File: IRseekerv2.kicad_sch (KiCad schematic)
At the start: 49 parts, among them J13 Conn_01x04_Pin, J14 Conn_01x02_Pin, J15 SEL_VOLTAGE, J16 G, J17 G, J18 G, J19 G, J20 Conn_01x02_Pin, J26 Conn_01x02_Pin, J27 Conn_01x02_Pin, J28 Conn_01x02_Pin, SW1 SW_Push, SW2 SW_Push, U10 TSSP4038, U11 TSSP4038, U12 TSSP4038, U13 TSSP4038, U14 TSSP4038, U15 TSSP4038, U16 TSSP4038, U17 AMS1117-3.3, U2 HEF4082BT, U3 STM32G431CBUx, U4 HEF4082BT, U5 TSSP4038, U6 TSSP4038, U7 TSSP4038, U8 TSSP4038, U9 TSSP4038, Y1 Crystal

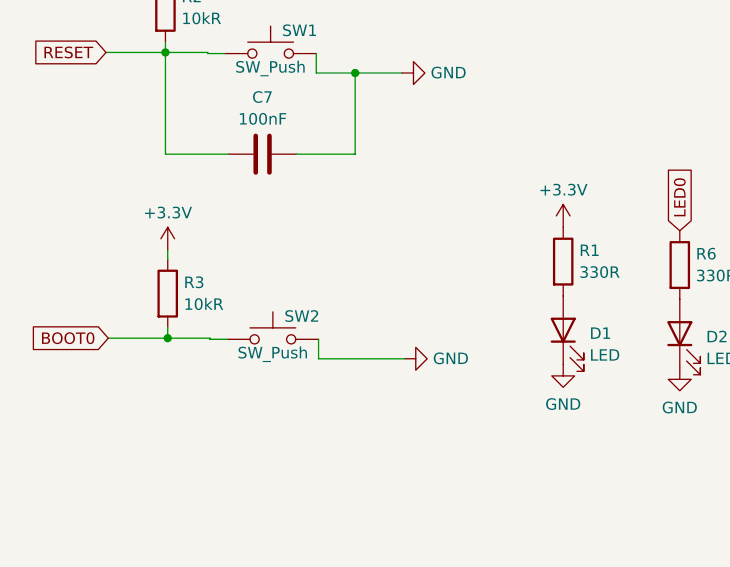
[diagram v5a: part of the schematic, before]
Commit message: BOOT0 pulldown instead of pullup
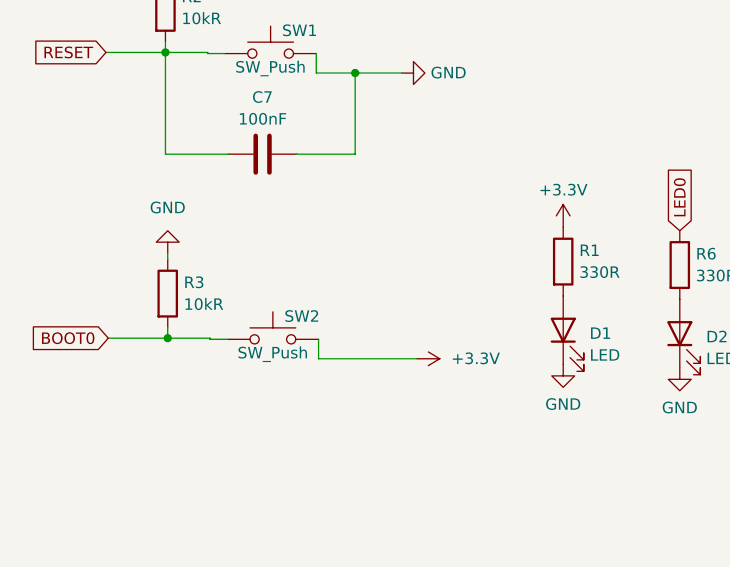
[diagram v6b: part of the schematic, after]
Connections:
- net +3.3V: now also SW2.2; no longer R3.1
- net GND: now also R3.1; no longer SW2.2
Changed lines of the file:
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@@
+    (stroke (width 0) (type default))
+  )
+  (wire (pts (xy 38.354 66.04) (xy 38.354 66.675))
     (stroke (width 0) (type default))
   )
@@
     (stroke (width 0) (type default))
   )
-  (wire (pts (xy 55.118 77.724) (xy 64.643 77.724))
+  (wire (pts (xy 55.118 77.724) (xy 66.04 77.724))
     (stroke (width 0) (type default))
   )
@@
   )
   (wire (pts (xy 226.695 149.479) (xy 226.695 158.623))
-    (stroke (width 0) (type default))
-  )
-  (wire (pts (xy 38.354 65.659) (xy 38.354 66.675))
     (stroke (width 0) (type default))
   )
@@
     )
   )
-  (symbol (lib_id "power:GND") (at 64.643 77.724 90) (unit 1)
-    (in_bom yes) (on_board yes) (dnp no) (fields_autoplaced)
-    (property "Reference" "#PWR017" (at 70.993 77.724 0)
-      (effects (font (size 1.27 1.27)) hide)
-    )
-    (property "Value" "GND" (at 67.818 77.724 90)
-      (effects (font (size 1.27 1.27)) (justify right))
-    )
-    (property "Footprint" "" (at 64.643 77.724 0)
-      (effects (font (size 1.27 1.27)) hide)
-    )
-    (property "Datasheet" "" (at 64.643 77.724 0)
-      (effects (font (size 1.27 1.27)) hide)
-    )
-    (pin "1")
-    (instances
-      (project "IRseekerv2"
-        (path "/c83ed66b-8f4f-4f32-bd83-eab9fc6ed48e"
-          (reference "#PWR017") (unit 1)
-        )
-      )
-    )
-  )
   (symbol (lib_id "Sensor_Proximity:TSSP58038") (at 257.937 139.192 270) (unit 1)
     (in_bom yes) (on_board yes) (dnp no) (fields_autoplaced)
@@
     )
   )
-  (symbol (lib_id "power:+3.3V") (at 38.354 65.659 0) (unit 1)
-    (in_bom yes) (on_board yes) (dnp no) (fields_autoplaced)
-    (property "Reference" "#PWR016" (at 38.354 69.469 0)
-      (effects (font (size 1.27 1.27)) hide)
-    )
-    (property "Value" "+3.3V" (at 38.354 61.5259 0)
-      (effects (font (size 1.27 1.27)))
-    )
-    (property "Footprint" "" (at 38.354 65.659 0)
-      (effects (font (size 1.27 1.27)) hide)
-    )
-    (property "Datasheet" "" (at 38.354 65.659 0)
+  (symbol (lib_id "power:+3.3V") (at 66.04 77.724 270) (unit 1)
+    (in_bom yes) (on_board yes) (dnp no) (fields_autoplaced)
+    (property "Reference" "#PWR016" (at 62.23 77.724 0)
+      (effects (font (size 1.27 1.27)) hide)
+    )
+    (property "Value" "+3.3V" (at 69.85 77.724 90)
+      (effects (font (size 1.27 1.27)) (justify left))
+    )
+    (property "Footprint" "" (at 66.04 77.724 0)
+      (effects (font (size 1.27 1.27)) hide)
+    )
+    (property "Datasheet" "" (at 66.04 77.724 0)
       (effects (font (size 1.27 1.27)) hide)
     )
@@
         )
       )
+    )
+  )
+  (symbol (lib_id "power:GND") (at 38.354 66.04 180) (unit 1)
+    (in_bom yes) (on_board yes) (dnp no) (fields_autoplaced)
+    (property "Reference" "#PWR027" (at 38.354 59.69 0)
+      (effects (font (size 1.27 1.27)) hide)
+    )
+    (property "Value" "GND" (at 38.354 60.96 0)
+      (effects (font (size 1.27 1.27)))
+    )
+    (property "Footprint" "" (at 38.354 66.04 0)
+      (effects (font (size 1.27 1.27)) hide)
+    )
+    (property "Datasheet" "" (at 38.354 66.04 0)
+      (effects (font (size 1.27 1.27)) hide)
+    )
+    (pin "1")
+    (instances
+      (project "IRseekerv2"
+        (path "/c83ed66b-8f4f-4f32-bd83-eab9fc6ed48e"
+          (reference "#PWR027") (unit 1)
+        )
+      )

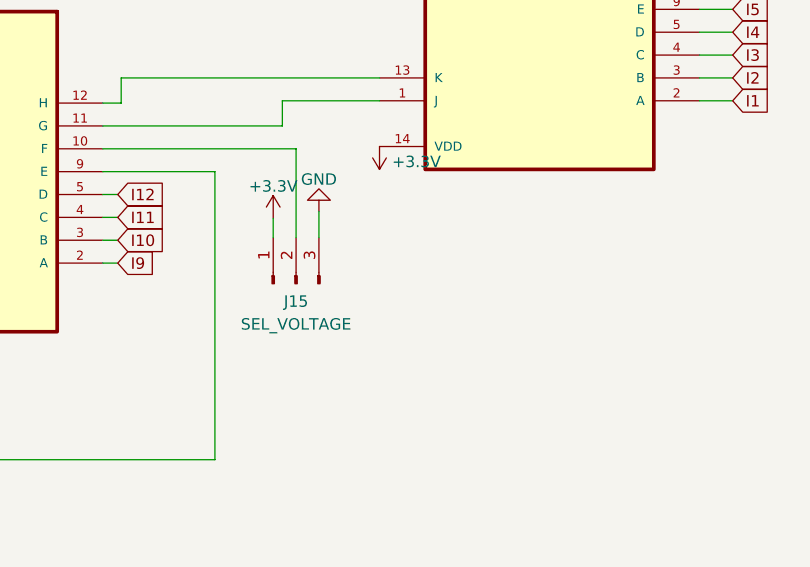
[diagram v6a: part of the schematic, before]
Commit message: removed SEL_VOlTAGE and added OUTGATE pin out
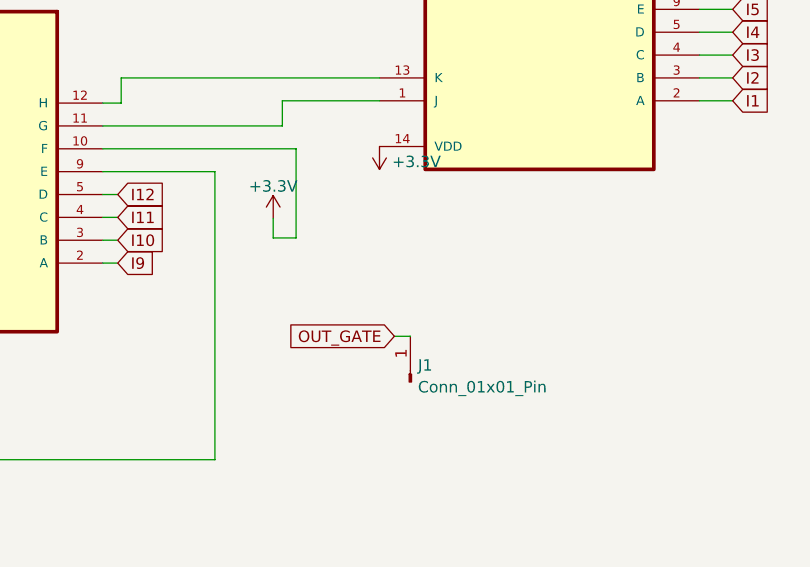
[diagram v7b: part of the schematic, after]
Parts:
- removed J15: SEL_VOLTAGE, Connector_PinHeader_2.54mm:PinHeader_1x03_P2.54mm_Vertical, symbol Connector:Conn_01x03_Male
- added J1: Conn_01x01_Pin, Connector_PinHeader_2.54mm:PinHeader_1x01_P2.54mm_Vertical, symbol Connector:Conn_01x01_Pin
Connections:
- net +3.3V: now also U2.10 (F)
- net OUT_GATE: now also J1.1 (Pin_1)
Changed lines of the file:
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@@
-    (stroke (width 0) (type default))
-  )
-  (wire (pts (xy 162.687 204.089) (xy 162.687 207.01))
     (stroke (width 0) (type default))
   )
@@
     (stroke (width 0) (type default))
   )
+  (wire (pts (xy 160.147 197.104) (xy 160.147 207.01))
+    (stroke (width 0) (type default))
+  )
   (wire (pts (xy 138.684 192.024) (xy 140.716 192.024))
     (stroke (width 0) (type default))
@@
     (stroke (width 0) (type default))
   )
+  (wire (pts (xy 171.069 217.932) (xy 172.847 217.932))
+    (stroke (width 0) (type default))
+  )
   (wire (pts (xy 329.946 94.742) (xy 329.946 93.98))
     (stroke (width 0) (type default))
@@
     (stroke (width 0) (type default))
   )
+  (wire (pts (xy 160.147 207.01) (xy 157.607 207.01))
+    (stroke (width 0) (type default))
+  )
   (wire (pts (xy 380.873 151.257) (xy 380.873 170.688))
     (stroke (width 0) (type default))
@@
     (stroke (width 0) (type default))
   )
-  (wire (pts (xy 160.147 197.104) (xy 160.147 207.01))
-    (stroke (width 0) (type default))
-  )
   (wire (pts (xy 165.1 67.31) (xy 177.8 67.31))
     (stroke (width 0) (type default))
@@
     (property "Intersheetrefs" "${INTERSHEET_REFS}" (at 362.4944 168.5766 0)
       (effects (font (size 1.27 1.27)) (justify left) hide)
+    )
+  )
+  (global_label "OUT_GATE" (shape input) (at 171.069 217.932 180) (fields_autoplaced)
+    (effects (font (size 1.27 1.27)) (justify right))
+    (property "Intersheetrefs" "${INTERSHEET_REFS}" (at 159.5845 217.8526 0)
+      (effects (font (size 1.27 1.27)) (justify right) hide)
     )
   )
@@
     )
   )
+  (symbol (lib_id "Connector:Conn_01x01_Pin") (at 172.847 223.012 90) (unit 1)
+    (in_bom yes) (on_board yes) (dnp no) (fields_autoplaced)
+    (property "Reference" "J1" (at 173.6852 221.1649 90)
+      (effects (font (size 1.27 1.27)) (justify right))
+    )
+    (property "Value" "Conn_01x01_Pin" (at 173.6852 223.5891 90)
+      (effects (font (size 1.27 1.27)) (justify right))
+    )
+    (property "Footprint" "Connector_PinHeader_2.54mm:PinHeader_1x01_P2.54mm_Vertical" (at 172.847 223.012 0)
+      (effects (font (size 1.27 1.27)) hide)
+    )
+    (property "Datasheet" "~" (at 172.847 223.012 0)
+      (effects (font (size 1.27 1.27)) hide)
+    )
+    (pin "1")
+    (instances
+      (project "IRseekerv2"
+        (path "/c83ed66b-8f4f-4f32-bd83-eab9fc6ed48e"
+          (reference "J1") (unit 1)
+        )
+      )
+    )
+  )
   (symbol (lib_id "power:+3.3V") (at 150.876 100.203 0) (unit 1)
     (in_bom yes) (on_board yes) (dnp no) (fields_autoplaced)
@@
         (path "/c83ed66b-8f4f-4f32-bd83-eab9fc6ed48e"
           (reference "#PWR0114") (unit 1)
-        )
-      )
-    )
-  )
-  (symbol (lib_id "Connector:Conn_01x03_Male") (at 160.147 212.09 90) (unit 1)
-    (in_bom yes) (on_board yes) (dnp no) (fields_autoplaced)
-    (property "Reference" "J15" (at 160.147 214.0696 90)
-      (effects (font (size 1.27 1.27)))
-    )
-    (property "Value" "SEL_VOLTAGE" (at 160.147 216.6065 90)
-      (effects (font (size 1.27 1.27)))
-    )
-    (property "Footprint" "Connector_PinHeader_2.54mm:PinHeader_1x03_P2.54mm_Vertical" (at 160.147 212.09 0)
-      (effects (font (size 1.27 1.27)) hide)
-    )
-    (property "Datasheet" "~" (at 160.147 212.09 0)
-      (effects (font (size 1.27 1.27)) hide)
-    )
-    (pin "1")
-    (pin "2")
-    (pin "3")
-    (instances
-      (project "IRseekerv2"
-        (path "/c83ed66b-8f4f-4f32-bd83-eab9fc6ed48e"
-          (reference "J15") (unit 1)
         )
       )
@@
         )
       )
-    )
-  )
-  (symbol (lib_id "power:GND") (at 162.687 204.089 180) (unit 1)
-    (in_bom yes) (on_board yes) (dnp no) (fields_autoplaced)
-    (property "Reference" "#PWR010" (at 162.687 197.739 0)
-      (effects (font (size 1.27 1.27)) hide)
-    )
-    (property "Value" "GND" (at 162.687 200.5132 0)
-      (effects (font (size 1.27 1.27)))
-    )
-    (property "Footprint" "" (at 162.687 204.089 0)
-      (effects (font (size 1.27 1.27)) hide)
-    )
-    (property "Datasheet" "" (at 162.687 204.089 0)
-      (effects (font (size 1.27 1.27)) hide)
-    )
-    (pin "1")
-    (instances
-      (project "IRseekerv2"
-        (path "/c83ed66b-8f4f-4f32-bd83-eab9fc6ed48e"
-          (reference "#PWR010") (unit 1)
-        )
-      )

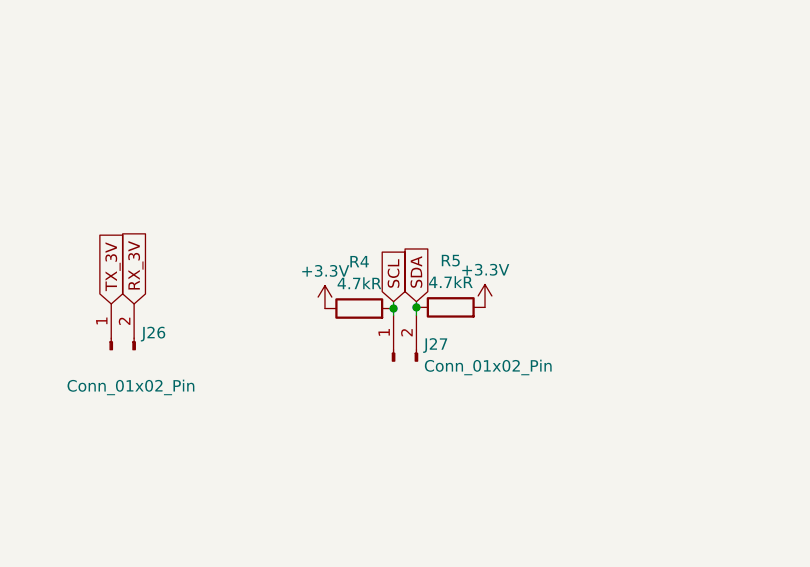
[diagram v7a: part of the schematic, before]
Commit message: change crystal to smd version
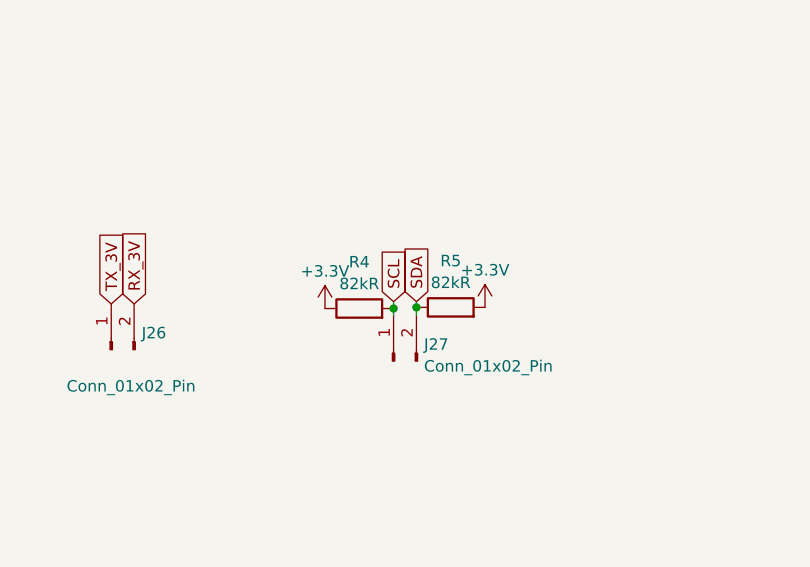
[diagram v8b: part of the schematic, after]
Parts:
- J1, J13, J14, J16, J17, J18, J19, J20, J26, J27, J28: now left out of the parts list
- R4, R5: value 4.7kR -> 82kR
- Y1: footprint Crystal:Crystal_HC49-4H_Vertical -> Crystal:Crystal_SMD_HC49-SD
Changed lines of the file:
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@@
   )
   (symbol (lib_id "Connector:Conn_01x02_Pin") (at 298.577 99.314 90) (unit 1)
-    (in_bom yes) (on_board yes) (dnp no)
+    (in_bom no) (on_board yes) (dnp no)
     (property "Reference" "J26" (at 301.9552 97.4669 90)
       (effects (font (size 1.27 1.27)) (justify right))
@@
   )
   (symbol (lib_id "Connector:Conn_01x04_Pin") (at 140.843 156.21 90) (unit 1)
-    (in_bom yes) (on_board yes) (dnp no) (fields_autoplaced)
+    (in_bom no) (on_board yes) (dnp no) (fields_autoplaced)
     (property "Reference" "J13" (at 142.113 157.8793 90)
       (effects (font (size 1.27 1.27)))
@@
   )
   (symbol (lib_id "Connector:Conn_01x01_Pin") (at 172.847 223.012 90) (unit 1)
-    (in_bom yes) (on_board yes) (dnp no) (fields_autoplaced)
+    (in_bom no) (on_board yes) (dnp no) (fields_autoplaced)
     (property "Reference" "J1" (at 173.6852 221.1649 90)
       (effects (font (size 1.27 1.27)) (justify right))
@@
   )
   (symbol (lib_id "Connector:Conn_01x02_Pin") (at 329.946 100.584 90) (unit 1)
-    (in_bom yes) (on_board yes) (dnp no) (fields_autoplaced)
+    (in_bom no) (on_board yes) (dnp no) (fields_autoplaced)
     (property "Reference" "J27" (at 333.3242 98.7369 90)
       (effects (font (size 1.27 1.27)) (justify right))
@@
       (effects (font (size 1.27 1.27)))
     )
-    (property "Value" "4.7kR" (at 336.296 91.8789 90)
+    (property "Value" "82kR" (at 336.296 91.8789 90)
       (effects (font (size 1.27 1.27)))
     )
@@
       (effects (font (size 1.27 1.27)))
     )
-    (property "Footprint" "Crystal:Crystal_HC49-4H_Vertical" (at 34.544 161.798 0)
+    (property "Footprint" "Crystal:Crystal_SMD_HC49-SD" (at 34.544 161.798 0)
       (effects (font (size 1.27 1.27)) hide)
     )
@@
   )
   (symbol (lib_id "Connector:Conn_01x02_Pin") (at 267.589 101.346 90) (unit 1)
-    (in_bom yes) (on_board yes) (dnp no) (fields_autoplaced)
+    (in_bom no) (on_board yes) (dnp no) (fields_autoplaced)
     (property "Reference" "J20" (at 270.9672 99.4989 90)
       (effects (font (size 1.27 1.27)) (justify right))
@@
   )
   (symbol (lib_id "Connector:Conn_01x01_Male") (at 215.138 249.555 0) (unit 1)
-    (in_bom yes) (on_board yes) (dnp no) (fields_autoplaced)
+    (in_bom no) (on_board yes) (dnp no) (fields_autoplaced)
     (property "Reference" "J17" (at 215.773 245.779 0)
       (effects (font (size 1.27 1.27)))
@@
   )
   (symbol (lib_id "Connector:Conn_01x01_Male") (at 215.138 263.271 0) (unit 1)
-    (in_bom yes) (on_board yes) (dnp no) (fields_autoplaced)
+    (in_bom no) (on_board yes) (dnp no) (fields_autoplaced)
     (property "Reference" "J19" (at 215.773 259.495 0)
       (effects (font (size 1.27 1.27)))
@@
   )
   (symbol (lib_id "Connector:Conn_01x01_Male") (at 214.63 255.016 0) (unit 1)
-    (in_bom yes) (on_board yes) (dnp no) (fields_autoplaced)
+    (in_bom no) (on_board yes) (dnp no) (fields_autoplaced)
     (property "Reference" "J16" (at 215.265 251.24 0)
       (effects (font (size 1.27 1.27)))
@@
   )
   (symbol (lib_id "Connector:Conn_01x02_Pin") (at 226.06 88.9 90) (unit 1)
-    (in_bom yes) (on_board yes) (dnp no) (fields_autoplaced)
+    (in_bom no) (on_board yes) (dnp no) (fields_autoplaced)
     (property "Reference" "J14" (at 229.4382 87.0529 90)
       (effects (font (size 1.27 1.27)) (justify right))
@@
       (effects (font (size 1.27 1.27)))
     )
-    (property "Value" "4.7kR" (at 326.136 92.0059 90)
+    (property "Value" "82kR" (at 326.136 92.0059 90)
       (effects (font (size 1.27 1.27)))
     )
@@
   )
   (symbol (lib_id "Connector:Conn_01x02_Pin") (at 225.552 106.172 90) (unit 1)
-    (in_bom yes) (on_board yes) (dnp no) (fields_autoplaced)
+    (in_bom no) (on_board yes) (dnp no) (fields_autoplaced)
     (property "Reference" "J28" (at 228.9302 104.3249 90)
       (effects (font (size 1.27 1.27)) (justify right))
@@
   )
   (symbol (lib_id "Connector:Conn_01x01_Male") (at 215.138 258.445 0) (unit 1)
-    (in_bom yes) (on_board yes) (dnp no)
+    (in_bom no) (on_board yes) (dnp no)
     (property "Reference" "J18" (at 212.344 258.572 0)
       (effects (font (size 1.27 1.27)))
